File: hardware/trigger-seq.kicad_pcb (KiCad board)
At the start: 2 copper layers, 80.8 x 104.6 mm, 65 parts, among them P1 CONN_02X05, P10 OUTS_MAIN, P3 COUNT_MAIN, P5 CLOCK_MAIN, P7 SWITCH_MAIN, P8 CONN_01X04, Q1 2N3904, Q2 2N3904, Q3 2N3904, Q4 2N3904, Q5 2N3906, Q6 2N3904, Q7 2N3906, U1 LM555N, U2 4029, U3 4051, U4 4051, U5 TL071, U6 LM358, U8 4081, U9 TL072

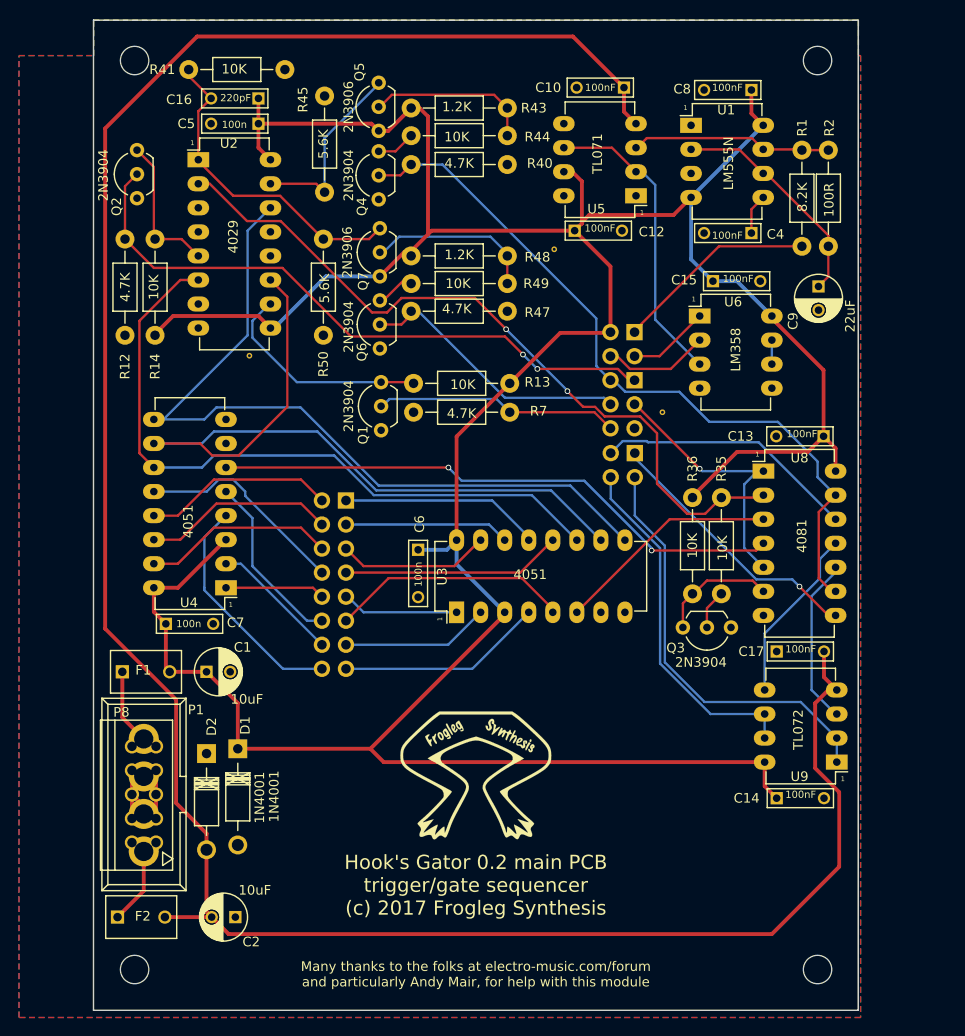
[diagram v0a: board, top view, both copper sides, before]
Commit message: replaced old hardware files with the most recent ones tracking CLAUDE.md AI files used in revising the project
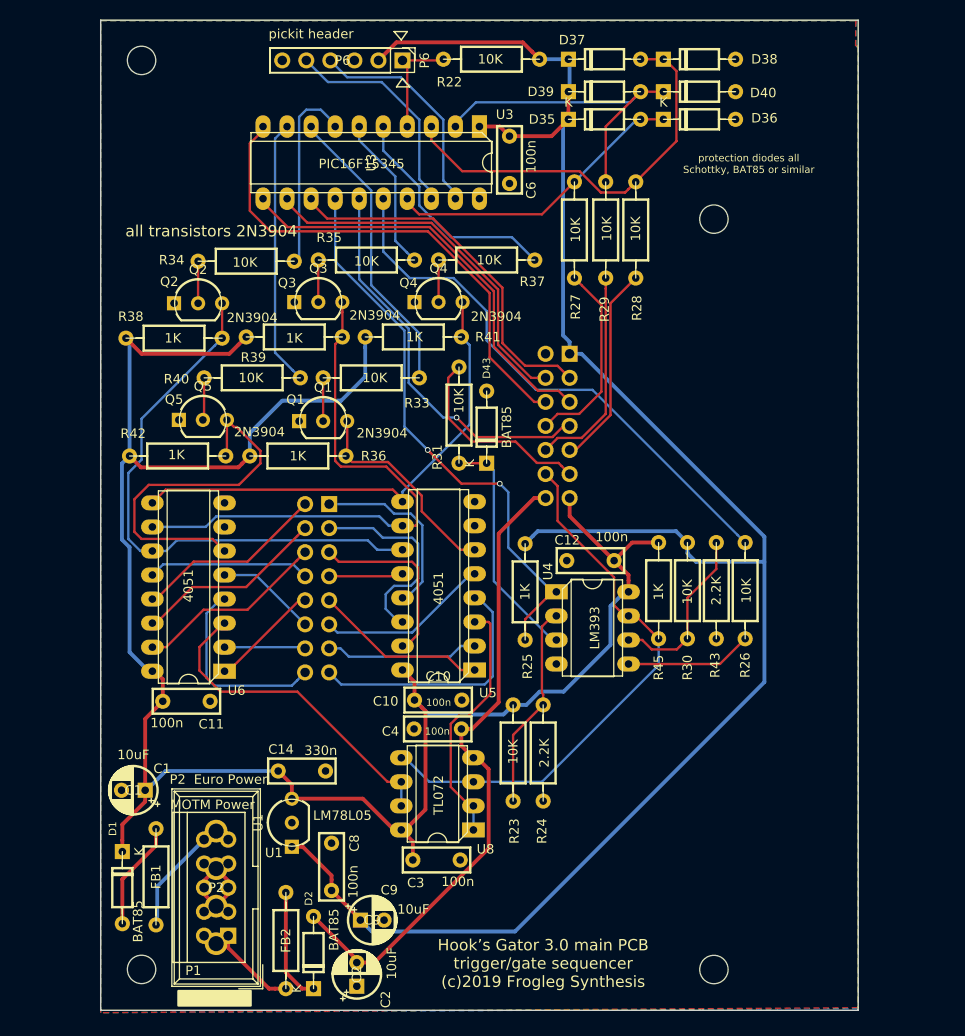
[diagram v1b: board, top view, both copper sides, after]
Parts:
- removed C13, C15, C17: 100nF, Capacitors_ThroughHole:C_Rect_L7_W2_P5
- removed C16: 220pF, Capacitors_ThroughHole:C_Rect_L7_W2_P5
- removed C5, C7: 100n, Capacitors_ThroughHole:C_Rect_L7_W2_P5
- removed F1, F2: F_Small, Capacitors_ThroughHole:C_Disc_D7.5_P5
- removed G***: LOGO, My Library:frogleg
- removed P10: OUTS_MAIN, Pin_Headers:Pin_Header_Straight_2x02
- removed P3: COUNT_MAIN, Pin_Headers:Pin_Header_Straight_2x03
- removed P5: CLOCK_MAIN, Pin_Headers:Pin_Header_Straight_2x02
- removed P8: CONN_01X04, My Library:MTA-156-4
- removed Q6: 2N3904, TO_SOT_Packages_THT:TO-92_Inline_Wide
- removed Q7: 2N3906, TO_SOT_Packages_THT:TO-92_Inline_Wide
- removed R1: 8.2K, Resistors_ThroughHole:Resistor_Horizontal_RM10mm
- removed R12, R47, R7: 4.7K, Resistors_ThroughHole:Resistor_Horizontal_RM10mm
- removed R13, R14, R44, R49: 10K, Resistors_ThroughHole:Resistor_Horizontal_RM10mm
- removed R2: 100R, Resistors_ThroughHole:Resistor_Horizontal_RM10mm
- removed R48: 1.2K, Resistors_ThroughHole:Resistor_Horizontal_RM10mm
- removed R50: 5.6K, Resistors_ThroughHole:Resistor_Horizontal_RM10mm
- removed the REF** at (129.6, 75.6)
- removed the REF** at (97.4, 86.8)
- removed the REF** at (85.2, 151.7)
- removed the REF** at (157.4, 55.6)
- removed the REF** at (141.0, 92.8)
- removed U2: 4029, Housings_DIP:DIP-16_W7.62mm_LongPads
- removed U9: TL072, Housings_DIP:DIP-8_W7.62mm_LongPads
- added C11: 100n, Capacitor_THT:C_Disc_D7.0mm_W2.5mm_P5.00mm, F.Cu at (88.2, 123.3)
- added C3: 100n, Capacitor_THT:C_Disc_D7.0mm_W2.5mm_P5.00mm, F.Cu at (114.6, 140.1)
- added D35: D_Schottky, Diode_THT:D_DO-35_SOD27_P7.62mm_Horizontal, F.Cu at (131.1, 61.8)
- added D36: D_Schottky, Diode_THT:D_DO-35_SOD27_P7.62mm_Horizontal, F.Cu at (141.1, 61.8)
- added D37: D_Schottky, Diode_THT:D_DO-35_SOD27_P7.62mm_Horizontal, F.Cu at (131.1, 55.5)
- added D38: D_Schottky, Diode_THT:D_DO-35_SOD27_P7.62mm_Horizontal, F.Cu at (141.1, 55.5)
- added D39: D_Schottky, Diode_THT:D_DO-35_SOD27_P7.62mm_Horizontal, F.Cu at (131.1, 58.9)
- added D40: D_Schottky, Diode_THT:D_DO-35_SOD27_P7.62mm_Horizontal, F.Cu at (141.1, 58.9)
- added D43: BAT85, Diode_THT:D_DO-35_SOD27_P7.62mm_Horizontal, F.Cu at (122.4, 98.2)
- added FB1: Ferrite_Bead_Small, Resistor_THT:R_Axial_DIN0207_L6.3mm_D2.5mm_P10.16mm_Horizontal, F.Cu at (87.5, 136.8)
- added FB2: Ferrite_Bead_Small, Resistor_THT:R_Axial_DIN0207_L6.3mm_D2.5mm_P10.16mm_Horizontal, F.Cu at (101.2, 143.5)
- added P2: Euro Power, Connector_IDC:IDC-Header_2x05_P2.54mm_Vertical, F.Cu at (95.1, 148.1)
- added P4: JACKS_MAIN, Connector_PinHeader_2.54mm:PinHeader_2x07_P2.54mm_Vertical, B.Cu at (131.2, 86.6)
- added P6: pickit header, Connector_PinHeader_2.54mm:PinHeader_1x06_P2.54mm_Vertical, F.Cu at (113.5, 55.6)
- added R22: 10K, Resistor_THT:R_Axial_DIN0207_L6.3mm_D2.5mm_P10.16mm_Horizontal, F.Cu at (128.0, 55.5)
- added R23: 10K, Resistor_THT:R_Axial_DIN0207_L6.3mm_D2.5mm_P10.16mm_Horizontal, F.Cu at (125.2, 123.7)
- added R24: 2.2K, Resistor_THT:R_Axial_DIN0207_L6.3mm_D2.5mm_P10.16mm_Horizontal, F.Cu at (128.4, 123.7)
- added R25: 1K, Resistor_THT:R_Axial_DIN0207_L6.3mm_D2.5mm_P10.16mm_Horizontal, F.Cu at (126.5, 106.7)
- added R26: 10K, Resistor_THT:R_Axial_DIN0207_L6.3mm_D2.5mm_P10.16mm_Horizontal, F.Cu at (149.7, 116.7)
- added R27: 10K, Resistor_THT:R_Axial_DIN0207_L6.3mm_D2.5mm_P10.16mm_Horizontal, F.Cu at (131.7, 68.5)
- added R28: 10K, Resistor_THT:R_Axial_DIN0207_L6.3mm_D2.5mm_P10.16mm_Horizontal, F.Cu at (138.2, 68.5)
- added R29: 10K, Resistor_THT:R_Axial_DIN0207_L6.3mm_D2.5mm_P10.16mm_Horizontal, F.Cu at (135.0, 68.5)
- added R30: 10K, Resistor_THT:R_Axial_DIN0207_L6.3mm_D2.5mm_P10.16mm_Horizontal, F.Cu at (143.6, 106.6)
- added R31: 10K, Resistor_THT:R_Axial_DIN0207_L6.3mm_D2.5mm_P10.16mm_Horizontal, F.Cu at (119.5, 98.2)
- added R33: 10K, Resistor_THT:R_Axial_DIN0207_L6.3mm_D2.5mm_P10.16mm_Horizontal, F.Cu at (105.2, 89.2)
- added R34: 10K, Resistor_THT:R_Axial_DIN0207_L6.3mm_D2.5mm_P10.16mm_Horizontal, F.Cu at (91.9, 76.8)
- added R37: 10K, Resistor_THT:R_Axial_DIN0207_L6.3mm_D2.5mm_P10.16mm_Horizontal, F.Cu at (117.3, 76.7)
- added R38: 1K, Resistor_THT:R_Axial_DIN0207_L6.3mm_D2.5mm_P10.16mm_Horizontal, F.Cu at (84.3, 85.0)
- added R39: 1K, Resistor_THT:R_Axial_DIN0207_L6.3mm_D2.5mm_P10.16mm_Horizontal, F.Cu at (97.0, 84.8)
- added R42: 1K, Resistor_THT:R_Axial_DIN0207_L6.3mm_D2.5mm_P10.16mm_Horizontal, F.Cu at (84.7, 97.4)
- added REF**: MountingHole_3mm, Mounting_Holes:MountingHole_3mm, F.Cu at (86.0, 151.6)
- added REF**: MountingHole_3mm, Mounting_Holes:MountingHole_3mm, F.Cu at (146.4, 72.4)
- C1, C2: footprint Capacitors_ThroughHole:C_Radial_D5_L6_P2.5 -> Capacitor_THT:CP_Radial_D5.0mm_P2.50mm
- C10, C12, C4, C8: value 100nF -> 100n; footprint Capacitors_ThroughHole:C_Rect_L7_W2_P5 -> Capacitor_THT:C_Disc_D7.0mm_W2.5mm_P5.00mm
- C14: value 100nF -> 330n; footprint Capacitors_ThroughHole:C_Rect_L7_W2_P5 -> Capacitor_THT:C_Disc_D7.0mm_W2.5mm_P5.00mm
- C6: footprint Capacitors_ThroughHole:C_Rect_L7_W2_P5 -> Capacitor_THT:C_Disc_D7.0mm_W2.5mm_P5.00mm
- C9: value 22uF -> 10uF; footprint Capacitors_ThroughHole:C_Radial_D5_L11_P2.5 -> Capacitor_THT:CP_Radial_D5.0mm_P2.50mm
- D1, D2: value 1N4001 -> BAT85; footprint Diodes_ThroughHole:Diode_DO-41_SOD81_Horizontal_RM10 -> Diode_THT:D_DO-35_SOD27_P7.62mm_Horizontal
- P1: value CONN_02X05 -> MOTM Power; footprint Connect:VASCH5x2 -> My Library:MTA-156
- P7: footprint Pin_Headers:Pin_Header_Straight_2x08 -> Connector_PinHeader_2.54mm:PinHeader_2x08_P2.54mm_Vertical
- Q1, Q2, Q3, Q4: footprint TO_SOT_Packages_THT:TO-92_Inline_Wide -> Package_TO_SOT_THT:TO-92_Inline_Wide
- Q5: value 2N3906 -> 2N3904; footprint TO_SOT_Packages_THT:TO-92_Inline_Wide -> Package_TO_SOT_THT:TO-92_Inline_Wide
- R35: footprint Resistors_ThroughHole:Resistor_Horizontal_RM10mm -> Resistor_THT:R_Axial_DIN0207_L6.3mm_D2.5mm_P10.16mm_Horizontal
- R36, R41: value 10K -> 1K; footprint Resistors_ThroughHole:Resistor_Horizontal_RM10mm -> Resistor_THT:R_Axial_DIN0207_L6.3mm_D2.5mm_P10.16mm_Horizontal
- R40: value 4.7K -> 10K; footprint Resistors_ThroughHole:Resistor_Horizontal_RM10mm -> Resistor_THT:R_Axial_DIN0207_L6.3mm_D2.5mm_P10.16mm_Horizontal
- R43: value 1.2K -> 2.2K; footprint Resistors_ThroughHole:Resistor_Horizontal_RM10mm -> Resistor_THT:R_Axial_DIN0207_L6.3mm_D2.5mm_P10.16mm_Horizontal
- R45: value 5.6K -> 1K; footprint Resistors_ThroughHole:Resistor_Horizontal_RM10mm -> Resistor_THT:R_Axial_DIN0207_L6.3mm_D2.5mm_P10.16mm_Horizontal
- U1: value LM555N -> LM78L05; footprint Housings_DIP:DIP-8_W7.62mm_LongPads -> Package_TO_SOT_THT:TO-92_Inline_Wide
- U3: value 4051 -> PIC16F15345; footprint Housings_DIP:DIP-16_W7.62mm_LongPads -> Package_DIP:DIP-20_W7.62mm_LongPads
- U4: value 4051 -> LM393; footprint Housings_DIP:DIP-16_W7.62mm_LongPads -> Package_DIP:DIP-8_W7.62mm_LongPads
- U5: value TL071 -> 4051; footprint Housings_DIP:DIP-8_W7.62mm_LongPads -> Package_DIP:DIP-16_W7.62mm_LongPads
- U6: value LM358 -> 4051; footprint Housings_DIP:DIP-8_W7.62mm_LongPads -> Package_DIP:DIP-16_W7.62mm_LongPads
- U8: value 4081 -> TL072; footprint Housings_DIP:DIP-14_W7.62mm_LongPads -> Package_DIP:DIP-8_W7.62mm_LongPads
- moved C8 95.5 mm to (106.0, 143.3), turned to 90 degrees
- moved U1 87.1 mm to (101.9, 138.7), turned to 90 degrees
- moved C9 82.6 mm to (109.1, 146.4), turned to 0 degrees
- moved C10 68.4 mm to (114.8, 123.2), turned to 0 degrees
- moved U6 62.7 mm to (94.7, 120.1), turned to 180 degrees
- moved C4 60.7 mm to (119.8, 126.2)
- moved R45 58.9 mm to (140.6, 106.6)
- moved Q3 57.5 mm to (102.1, 81.2), turned to 0 degrees
- moved U5 52.9 mm to (121.2, 120.0)
- moved C14 52.7 mm to (100.4, 130.7)
- moved U3 51.4 mm to (121.7, 62.6), turned to -90 degrees
- moved R43 50.9 mm to (146.7, 106.6), turned to -90 degrees
- moved R35 49.4 mm to (104.6, 76.7), turned to 0 degrees
- moved R36 49.0 mm to (97.4, 97.4), turned to 0 degrees
- moved U8 48.7 mm to (121.0, 136.9), turned to 180 degrees
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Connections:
- C10 pad 1: -12V -> +12V
- C4 pad 1: Net-(C4-Pad1) -> -12V
- C6 pad 1: +12V -> +5V
- C8 pad 1: +12V -> +5V
- C9 pad 1: Net-(C9-Pad1) -> +5V
- D1 pad 2: GND -> Net-(D1-Pad2)
- D2 pad 1: GND -> Net-(D2-Pad1)
- P1 pad 1: Net-(F2-Pad1) -> Net-(FB1-Pad2)
- P1 pad 2: Net-(F2-Pad1) -> GND
- P1 pad 4: GND -> Net-(FB2-Pad2)
- P7 pad 1: /main/counter/S1 -> /main/outputs/S1
- P7 pad 10: /main/counter/S13 -> /main/outputs/S13
- P7 pad 11: /main/counter/S6 -> /main/outputs/S6
- P7 pad 12: /main/counter/S14 -> /main/outputs/S14
- P7 pad 13: /main/counter/S7 -> /main/outputs/S7
- P7 pad 14: /main/counter/S15 -> /main/outputs/S15
- P7 pad 15: /main/counter/S8 -> /main/outputs/S8
- P7 pad 16: /main/counter/S16 -> /main/outputs/S16
- P7 pad 2: /main/counter/S9 -> /main/outputs/S9
- P7 pad 3: /main/counter/S2 -> /main/outputs/S2
- P7 pad 4: /main/counter/S10 -> /main/outputs/S10
- P7 pad 5: /main/counter/S3 -> /main/outputs/S3
- P7 pad 6: /main/counter/S11 -> /main/outputs/S11
- P7 pad 7: /main/counter/S4 -> /main/outputs/S4
- P7 pad 8: /main/counter/S12 -> /main/outputs/S12
- P7 pad 9: /main/counter/S5 -> /main/outputs/S5
- Q4 pad 2: /main/counter/PROC_CLK -> Net-(Q4-Pad2)
- Q5 pad 1: +12V -> GND
- Q5 pad 3: /main/counter/clock processing/clock.out -> Net-(Q5-Pad3)
- R35 pad 1: Net-(R35-Pad1) -> Net-(Q3-Pad2)
- R35 pad 2: Net-(Q3-Pad2) -> /main/clock/adr2
- R36 pad 1: Net-(Q3-Pad3) -> +12V
- R36 pad 2: +12V -> Net-(Q1-Pad3)
- R40 pad 1: GND -> Net-(Q5-Pad2)
- R40 pad 2: /main/counter/PROC_CLK -> /main/clock/inh2
- R41 pad 1: GND -> +12V
- R41 pad 2: /main/counter/reset processing/reset.out -> Net-(Q4-Pad3)
- R43 pad 1: Net-(Q5-Pad2) -> Net-(R30-Pad2)
- R43 pad 2: +12V -> GND
- R45 pad 1: GND -> +12V
- R45 pad 2: /main/counter/clock processing/clock.out -> /main/clock/ckbuf
- U1 pad 1: GND -> +5V
- U1 pad 2: Net-(C9-Pad1) -> GND
- U1 pad 3: (no net) -> +12V
- U3 pad 1: /main/counter/S5 -> +5V
- U3 pad 10: Net-(U2-Pad11) -> swing
- U3 pad 11: Net-(U2-Pad6) -> steps
- U3 pad 12: /main/counter/S4 -> rate
- U3 pad 13: /main/counter/S1 -> width
- U3 pad 14: /main/counter/S2 -> CKINBUF
- U3 pad 15: /main/counter/S3 -> 2x8/1x16
- U3 pad 16: +12V -> Net-(R26-Pad2)
- U3 pad 2: /main/counter/S7 -> Net-(D39-Pad2)
- U3 pad 3: +12V -> Net-(D37-Pad2)
- U3 pad 4: /main/counter/S8 -> pg
- U3 pad 5: /main/counter/S6 -> /main/clock/adr3
- U3 pad 6: Net-(U3-Pad6) -> /main/clock/adr2
- U3 pad 7: GND -> /main/clock/adr1
- U3 pad 8: GND -> /main/clock/inh1
- U3 pad 9: Net-(U2-Pad14) -> /main/clock/inh2
- U4 pad 1: /main/counter/S13 -> CKINBUF
- U4 pad 2: /main/counter/S15 -> Net-(R23-Pad2)
- U4 pad 3: +12V -> Net-(D43-Pad1)
- U4 pad 4: /main/counter/S16 -> GND
- U4 pad 5: /main/counter/S14 -> Net-(R26-Pad1)
- U4 pad 6: Net-(U4-Pad6) -> Net-(R30-Pad2)
- U4 pad 7: GND -> /main/clock/ckbuf
- U4 pad 8: GND -> +12V
- U5 pad 1: (no net) -> /main/outputs/S5
- U5 pad 2: Net-(U5-Pad2) -> /main/outputs/S7
- U5 pad 3: Net-(R1-Pad2) -> Net-(U5-Pad3)
- U5 pad 4: -12V -> /main/outputs/S8
- U5 pad 5: (no net) -> /main/outputs/S6
- U5 pad 6: Net-(U5-Pad2) -> Net-(Q1-Pad3)
- U5 pad 7: +12V -> GND
- U5 pad 8: (no net) -> GND
- U6 pad 1: /main/clock/INT_CLK -> /main/outputs/S13
- U6 pad 2: Net-(P4-Pad4) -> /main/outputs/S15
- U6 pad 3: Net-(U5-Pad2) -> Net-(U6-Pad3)
- U6 pad 4: GND -> /main/outputs/S16
- U6 pad 5: GND -> /main/outputs/S14
- U6 pad 6: Net-(U6-Pad6) -> Net-(Q5-Pad3)
- U6 pad 7: Net-(U6-Pad6) -> GND
- U6 pad 8: +12V -> GND
- U8 pad 1: Net-(P2-Pad3) -> Net-(U5-Pad3)
- U8 pad 2: Net-(R35-Pad1) -> Net-(U5-Pad3)
- U8 pad 3: Net-(U3-Pad6) -> /main/clock/ckbuf
- U8 pad 4: Net-(U4-Pad6) -> -12V
- U8 pad 5: Net-(P2-Pad3) -> /main/clock/ckbuf
- U8 pad 6: Net-(Q3-Pad3) -> Net-(U6-Pad3)
- U8 pad 7: GND -> Net-(U6-Pad3)
- U8 pad 8: /main/counter/1ST8 -> +12V
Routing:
- net +5V: track 0.00 -> 201.2 mm
- net -12V: track 254.1 -> 69.2 mm
- net +12V: track 350.5 -> 210.9 mm
- net Net-(U2-Pad14): track 84.1 -> 0.00 mm
- net Net-(U2-Pad11): track 83.4 -> 0.00 mm
- net /main/counter/PROC_CLK: track 79.4 -> 0.00 mm
- net Net-(R35-Pad1): track 79.4 -> 0.00 mm, vias 2 -> 0
- net Net-(U2-Pad6): track 73.0 -> 0.00 mm
- net Net-(Q2-Pad2): track 67.7 -> 4.45 mm, vias 2 -> 0
- net Net-(U4-Pad6): track 60.9 -> 0.00 mm, vias 2 -> 0
- net CKINBUF: track 0.00 -> 60.5 mm, vias 0 -> 2
- net /main/clock/ckbuf: track 0.00 -> 59.2 mm
- net Net-(R26-Pad2): track 0.00 -> 58.4 mm
- net swing: track 0.00 -> 53.0 mm
- net Net-(Q4-Pad3): track 4.11 -> 52.1 mm
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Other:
- board size 80.8 x 104.6 mm -> 80 x 104.6 mm
- net class Default removed
- net class power removed
- board text added: "Hook’s Gator 3.0 main PCB trigger/gate sequencer (c)2019 Frogleg Synthesis"
- board text added: "all transistors 2N3904"
- board text added: "protection diodes all Schottky, BAT85 or similar"
- board text added: "red stripe"
- board text removed: "1"
- board text removed: "Hook's Gator 0.2 main PCB trigger/gate sequencer (c) 2017 Frogleg Synthesis"
- board text removed: "Many thanks to the folks at electro-music.com/forum and particularly Andy Mair, for help with this module"

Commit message: expanding panel to 18HP so the controls are less crowded
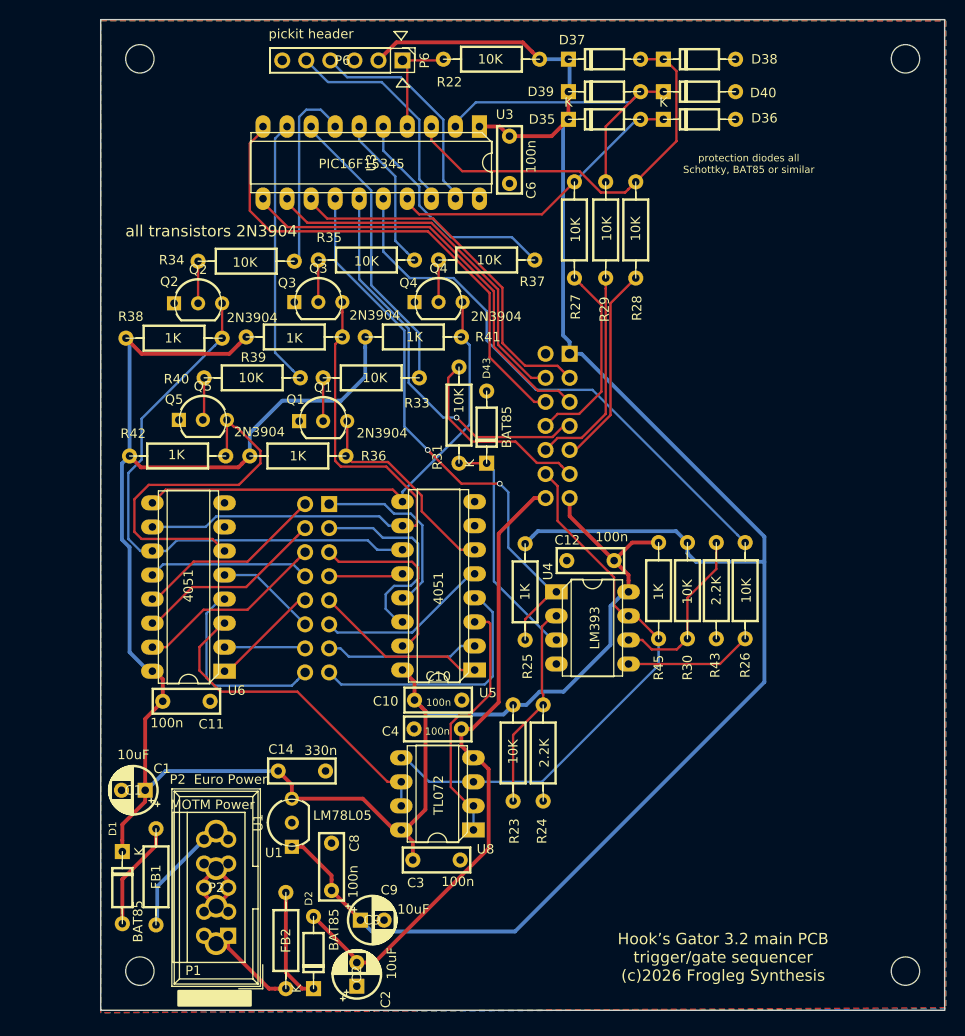
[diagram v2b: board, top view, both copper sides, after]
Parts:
- moved REF** 26.4 mm to (166.7, 55.5)
- moved REF** 20.2 mm to (166.7, 151.8)
- moved REF** 0.25 mm to (85.8, 151.8)
- moved REF** 0.25 mm to (85.8, 55.5)
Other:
- board size 80 x 104.6 mm -> 89.1 x 104.6 mm
- board text added: "Hook’s Gator 3.2 main PCB trigger/gate sequencer (c)2026 Frogleg Synthesis"
- board text removed: "Hook’s Gator 3.0 main PCB trigger/gate sequencer (c)2019 Frogleg Synthesis"
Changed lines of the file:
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@@
   (net 63 "Net-(R30-Pad2)")
   (footprint "Mounting_Holes:MountingHole_3mm" locked (layer "F.Cu")
-    (at 146.431 151.6507)
+    (at 166.665 151.818)
     (descr "Mounting hole, Befestigungsbohrung, 3mm, No Annular, Kein Restring,")
     (tags "Mounting hole, Befestigungsbohrung, 3mm, No Annular, Kein Restring,")
@@
   )
   (footprint "Mounting_Holes:MountingHole_3mm" locked (layer "F.Cu")
-    (at 85.979 55.626)
+    (at 85.799 55.458)
     (descr "Mounting hole, Befestigungsbohrung, 3mm, No Annular, Kein Restring,")
     (tags "Mounting hole, Befestigungsbohrung, 3mm, No Annular, Kein Restring,")
@@
   )
   (footprint "Mounting_Holes:MountingHole_3mm" locked (layer "F.Cu")
-    (at 85.979 151.638)
+    (at 85.799 151.818)
     (descr "Mounting hole, Befestigungsbohrung, 3mm, No Annular, Kein Restring,")
     (tags "Mounting hole, Befestigungsbohrung, 3mm, No Annular, Kein Restring,")
@@
   )
   (footprint "Mounting_Holes:MountingHole_3mm" locked (layer "F.Cu")
-    (at 146.431 72.39)
+    (at 166.665 55.458)
     (descr "Mounting hole, Befestigungsbohrung, 3mm, No Annular, Kein Restring,")
     (tags "Mounting hole, Befestigungsbohrung, 3mm, No Annular, Kein Restring,")
@@
   (gr_line (start 112.649 52.578) (end 114.046 52.578) (layer "F.SilkS") (width 0.15))
   (gr_line (start 113.411 53.467) (end 112.649 52.578) (layer "F.SilkS") (width 0.15))
-  (gr_line (start 161.671 155.956) (end 81.661 155.956) (layer "Edge.Cuts") (width 0.15))
-  (gr_line (start 161.671 51.3715) (end 161.671 155.956) (layer "Edge.Cuts") (width 0.15))
-  (gr_line (start 161.671 51.3715) (end 81.661 51.3715) (layer "Edge.Cuts") (width 0.15))
-  (gr_line (start 81.661 51.3715) (end 81.661 155.956) (layer "Edge.Cuts") (width 0.15))
-  (gr_text "Hook’s Gator 3.0 main PCB\ntrigger/gate sequencer\n(c)2019 Frogleg Synthesis" (at 128.397 151.003) (layer "F.SilkS")
+  (gr_line (start 170.803 155.956) (end 81.661 155.956) (layer "Edge.Cuts") (width 0.15))
+  (gr_line (start 170.803 51.32) (end 170.803 155.956) (layer "Edge.Cuts") (width 0.15))
+  (gr_line (start 170.803 51.32) (end 81.661 51.32) (layer "Edge.Cuts") (width 0.15))
+  (gr_line (start 81.661 51.32) (end 81.661 155.956) (layer "Edge.Cuts") (width 0.15))
+  (gr_text "Hook’s Gator 3.2 main PCB\ntrigger/gate sequencer\n(c)2026 Frogleg Synthesis" (at 147.404 150.355) (layer "F.SilkS")
     (effects (font (size 1.2 1.2) (thickness 0.25)))
   )
@@
     (polygon
       (pts
-        (xy 161.392867 54.079143)
-        (xy 161.621467 54.079143)
-        (xy 161.621467 155.679143)
+        (xy 161.62075 51.445372)
+        (xy 170.901874 51.443287)
+        (xy 170.902467 155.679143)
         (xy 81.661 156.21)
         (xy 81.661 54.61)
         (xy 81.661 53.467)
         (xy 81.661 51.435)
-        (xy 161.417 51.435)
+        (xy 161.645476 51.437085)
       )
     )
@@
     (polygon
       (pts
-        (xy 161.435385 54.170897)
-        (xy 161.663985 54.170897)
-        (xy 161.663985 155.770897)
+        (xy 161.661515 51.435735)
+        (xy 170.936432 51.437252)
+        (xy 170.935985 155.770897)
         (xy 81.661 156.21)
         (xy 81.661 54.61)
         (xy 81.661 53.467)
         (xy 81.661 51.435)
-        (xy 161.417 51.435)
+        (xy 161.642683 51.433483)
       )
     )

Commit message: wider panel + better spacing v3.3
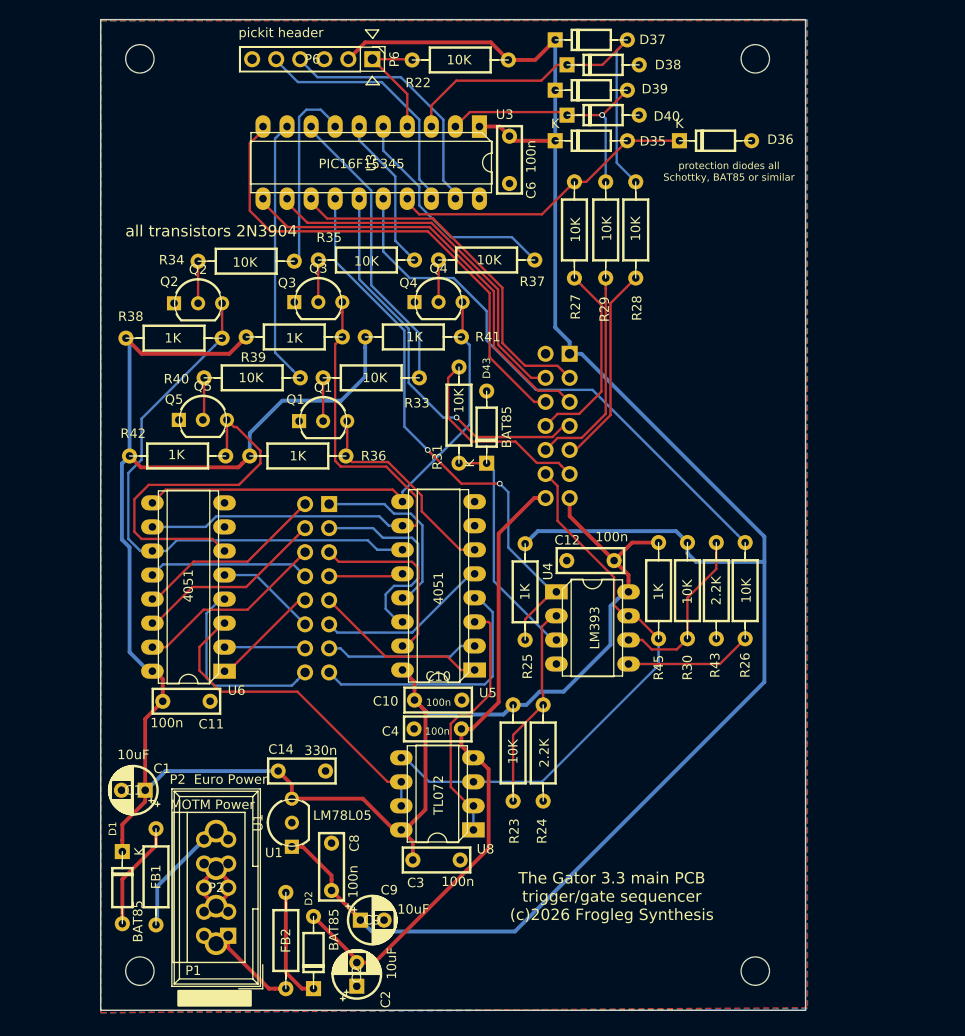
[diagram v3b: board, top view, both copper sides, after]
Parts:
- moved REF** 15.9 mm to (150.8, 151.8)
- moved REF** 15.9 mm to (150.8, 55.5)
- moved D40 10.5 mm to (130.9, 61.4)
- moved D38 10.2 mm to (130.9, 56.1)
- moved R22 3.30 mm to (124.7, 55.6)
- moved P6 3.18 mm to (110.4, 55.5)
- moved D36 2.83 mm to (142.8, 64.1)
- moved D35 2.66 mm to (129.7, 64.1)
- moved D37 2.47 mm to (129.7, 53.5)
- moved D39 1.40 mm to (129.7, 58.8)
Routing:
- net Net-(D39-Pad2): track 34.9 -> 27.6 mm, vias 0 -> 1
- net pgck: track 23.4 -> 26.7 mm
- net pgdt: track 23.4 -> 26.7 mm
- net +5V: track 201.2 -> 203.9 mm
- net Net-(D37-Pad2): track 43.5 -> 42.1 mm
- net pg: track 11.6 -> 12.9 mm
- net Net-(D35-Pad2): track 32.1 -> 32.9 mm
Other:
- board size 89.1 x 104.6 mm -> 74.5 x 104.6 mm
- board text added: "The Gator 3.3 main PCB trigger/gate sequencer (c)2026 Frogleg Synthesis"
- board text removed: "Hook’s Gator 3.2 main PCB trigger/gate sequencer (c)2026 Frogleg Synthesis"

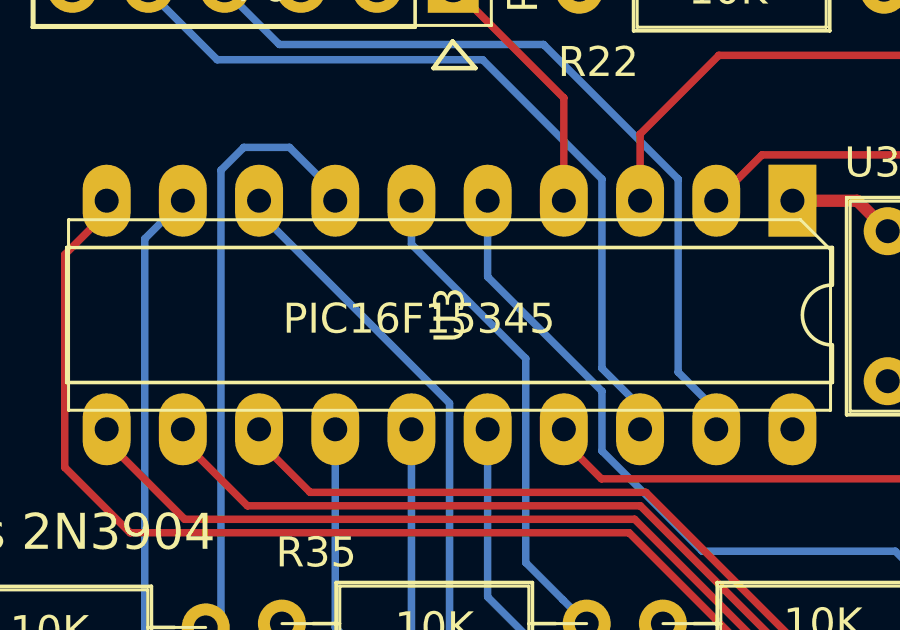
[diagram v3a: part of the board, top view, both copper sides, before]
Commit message: update for version 3.3, slight tweaks to v3.2 which has now passed smoke test.
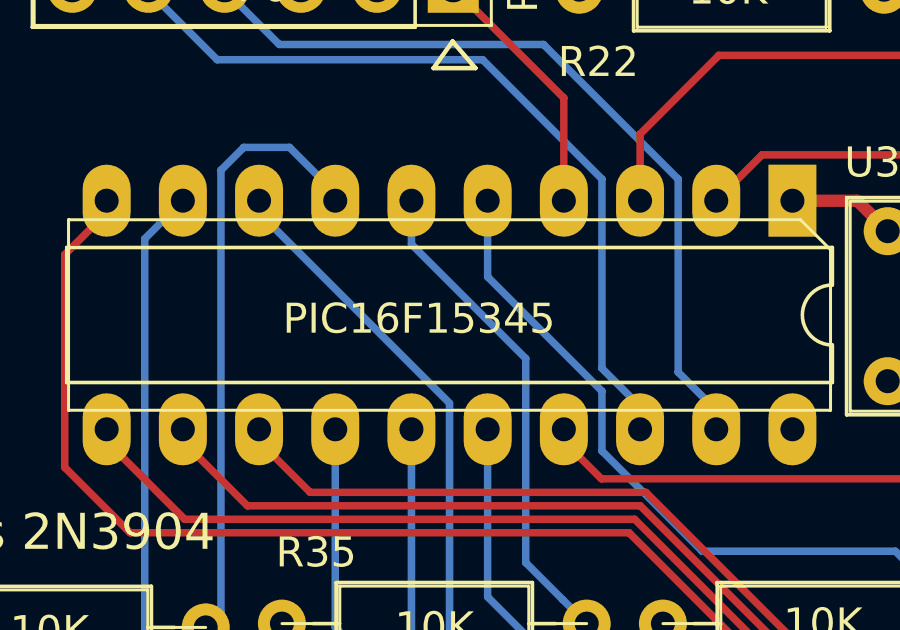
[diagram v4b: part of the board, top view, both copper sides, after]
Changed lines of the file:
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@@
       (effects (font (size 1 1) (thickness 0.15)))
     )
-    (fp_text user "${REFERENCE}" (at 3.81 11.43 -90) (layer "F.SilkS")
+    (fp_text user "${REFERENCE}" (at 3.81 11.43 -90) (layer "F.SilkS") hide
       (effects (font (size 1 1) (thickness 0.15)))
     )
